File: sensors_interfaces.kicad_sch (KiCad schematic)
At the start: 39 parts, among them IC1 PCF8563T_5,518, IC2 W25Q128JVSIQTR, IC5 SP3485EN-L_TR, IC8 STK8321, U1 TMP112xxDRL, U2 DAC5571IDBVR, U3 DAC5571IDBVR, X14 CH340G, X2 32.768 kHz, X3 TF-15×15, X4 CR1220-2ZX, Y1 X322512MSB4SI

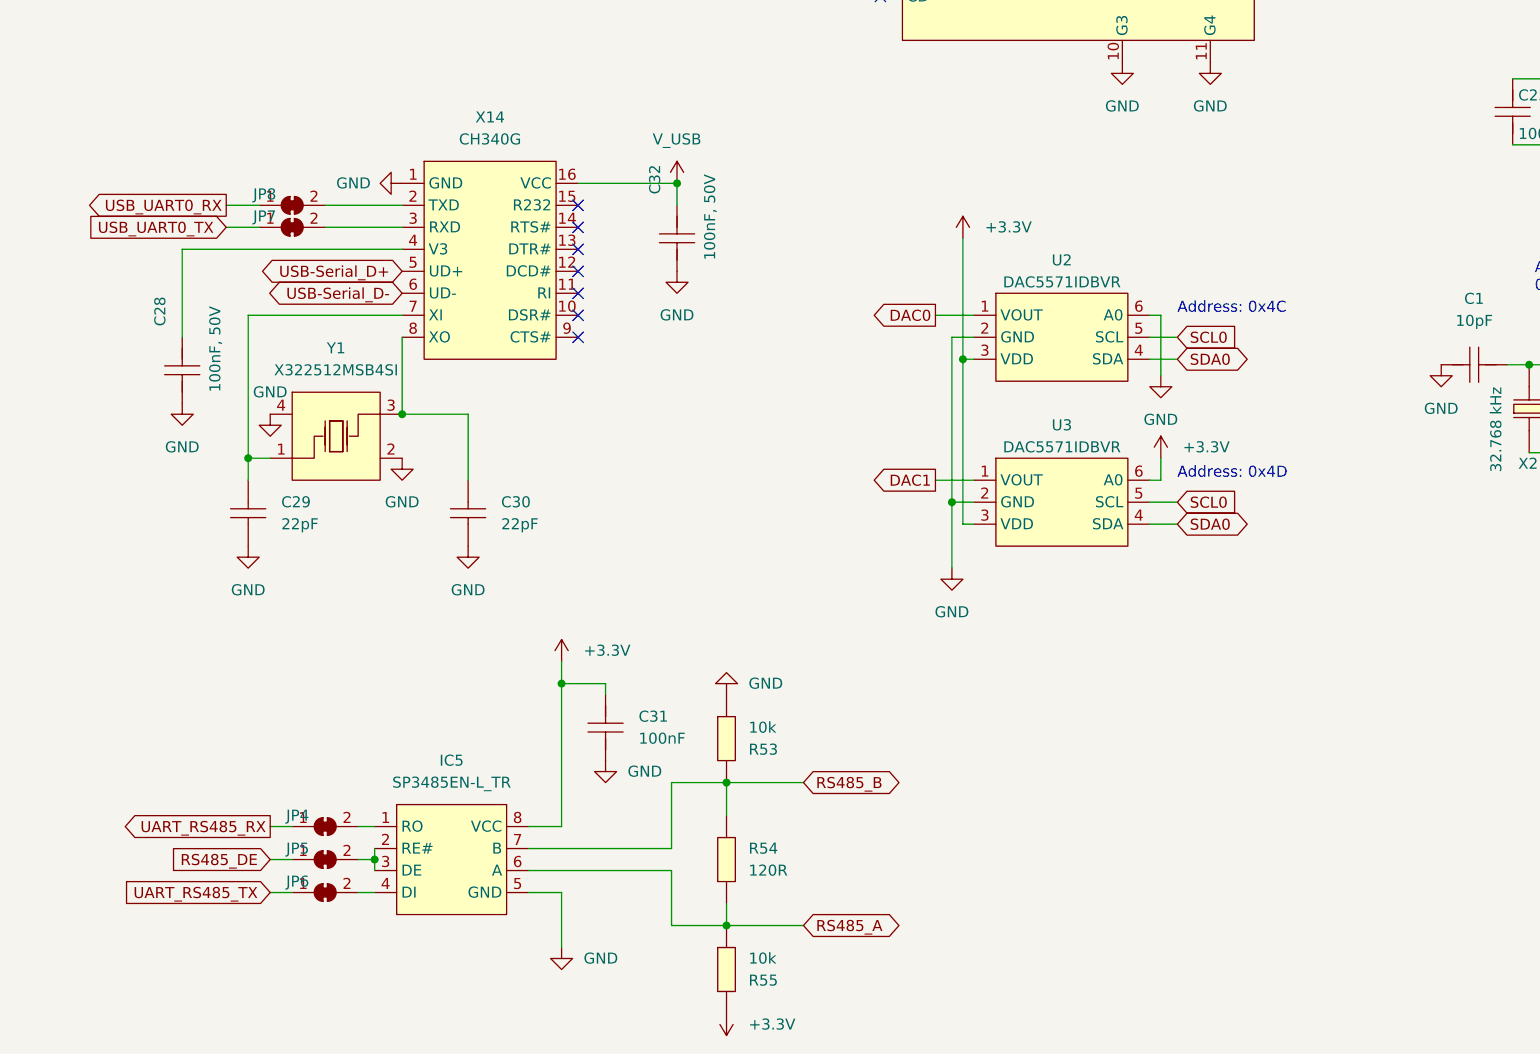
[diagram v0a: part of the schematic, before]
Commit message: Sort out RX/TX problems, improve DAC Circuits, Improve Board Text, switch out certain solder-jumpers with resistors
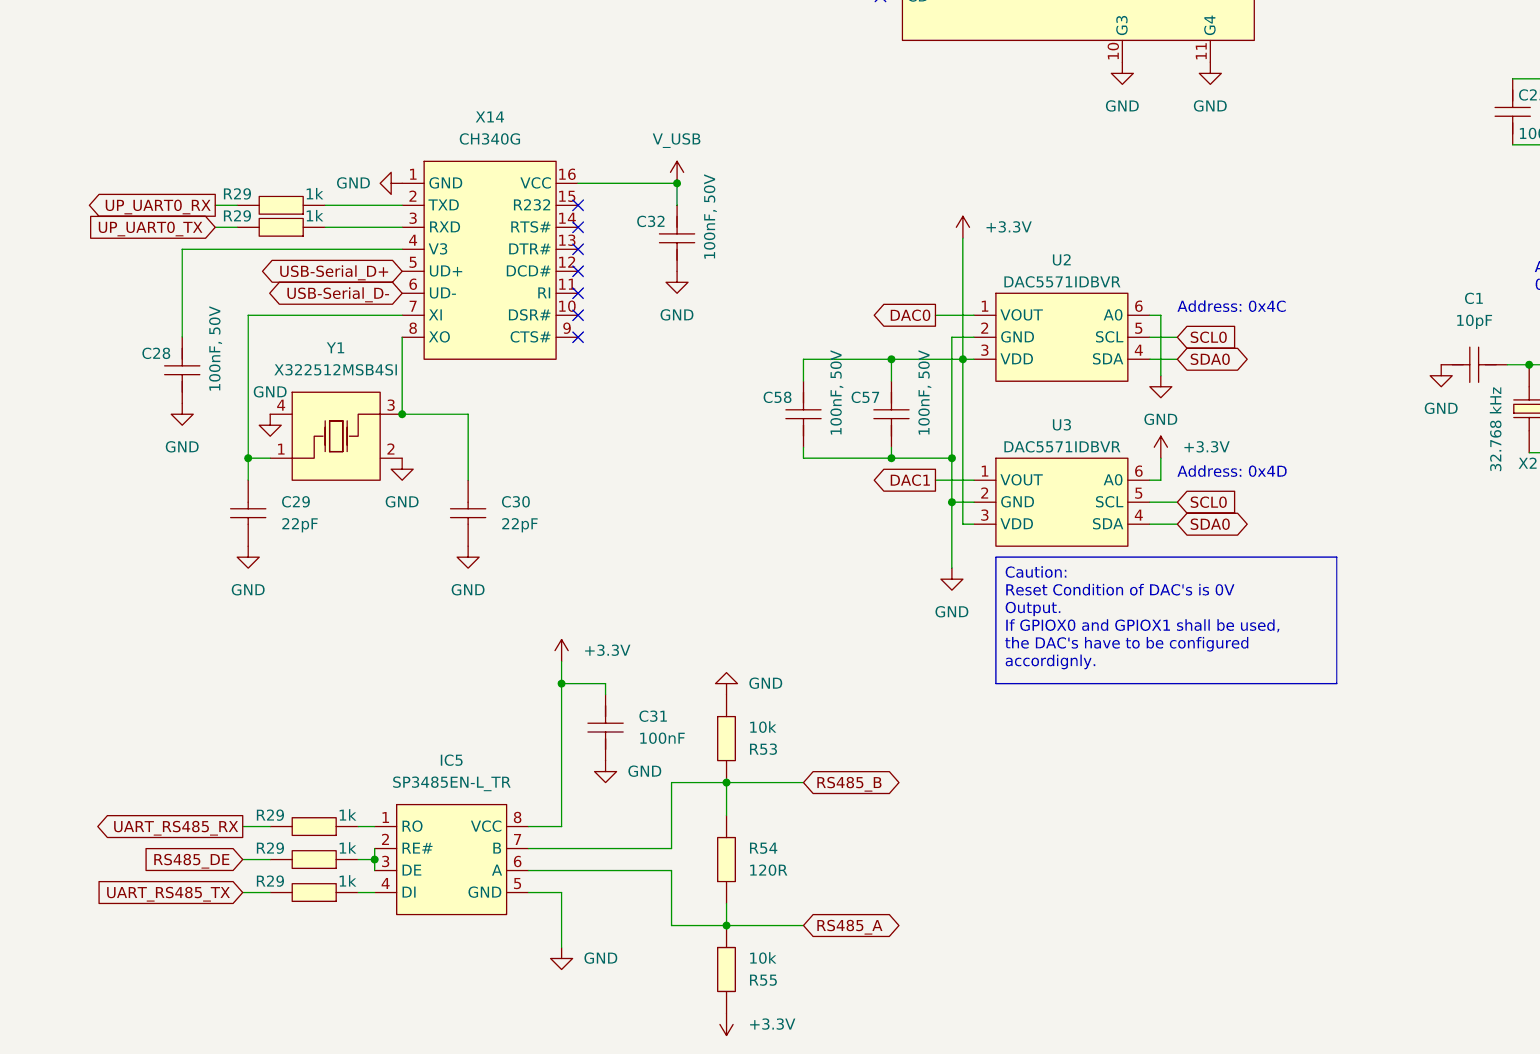
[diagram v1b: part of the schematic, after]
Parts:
- removed JP4, JP5, JP6, JP7, JP8: SolderJumper_2_Bridged, Jumper:SolderJumper-2_P1.3mm_Bridged_Pad1.0x1.5mm, symbol Jumper:SolderJumper_2_Bridged
- added C57, C58: 100nF, 50V, Capacitor_SMD:C_0402_1005Metric_Pad0.74x0.62mm_HandSolder, symbol eduboardv2:CL05B104KB54PNC
- added R29 (x5): 1k, Resistor_SMD:R_0402_1005Metric_Pad0.72x0.64mm_HandSolder, symbol eduboardv2:0402WGF1001TCE
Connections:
- net +3.3V: now also C57.2, C58.2
- net GND: now also C57.1, C58.1
- net RS485_DE: now also R29.2
- net UART_RS485_RX: now also R29.2
- net UART_RS485_TX: now also R29.2
- net at IC5.1 (RO): now also R29.1
- net at IC5.2 (RE#), IC5.3 (DE): now also R29.1
- net at IC5.4 (DI): now also R29.1
- net at X14.3 (RXD): now also R29.1
- net at X14.2 (TXD): now also R29.1
- new net UP_UART0_RX: R29.2
- new net UP_UART0_TX: R29.2

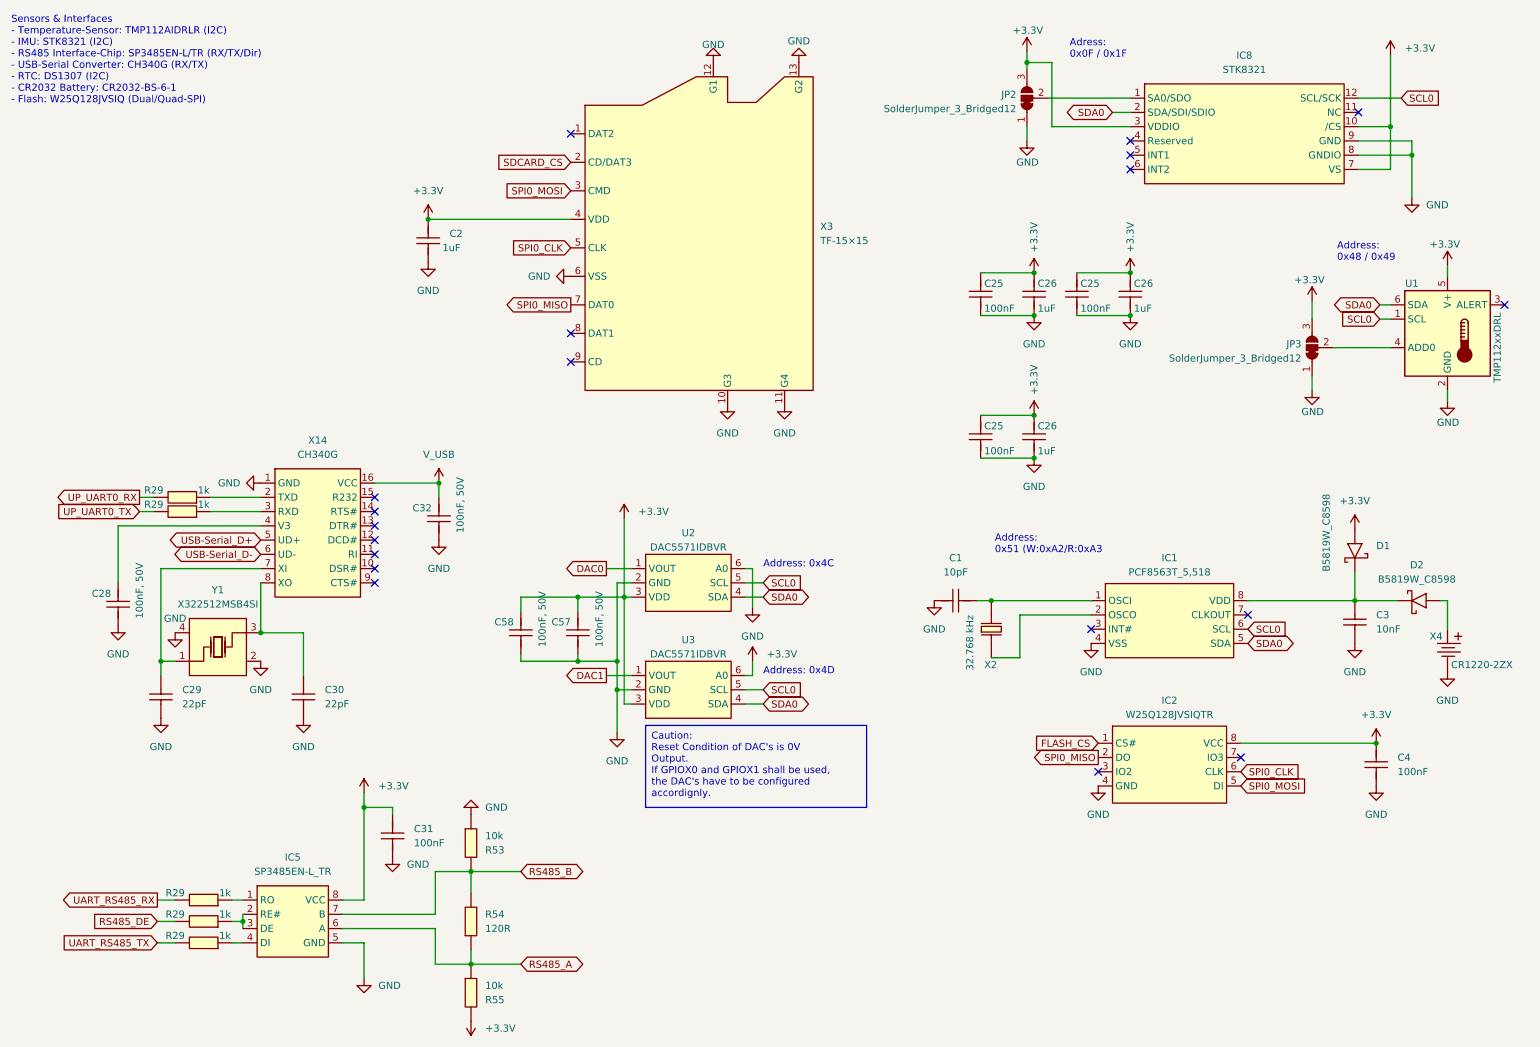
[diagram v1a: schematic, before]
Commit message: replace DAC with SPI Variant. Set Version to 2.2
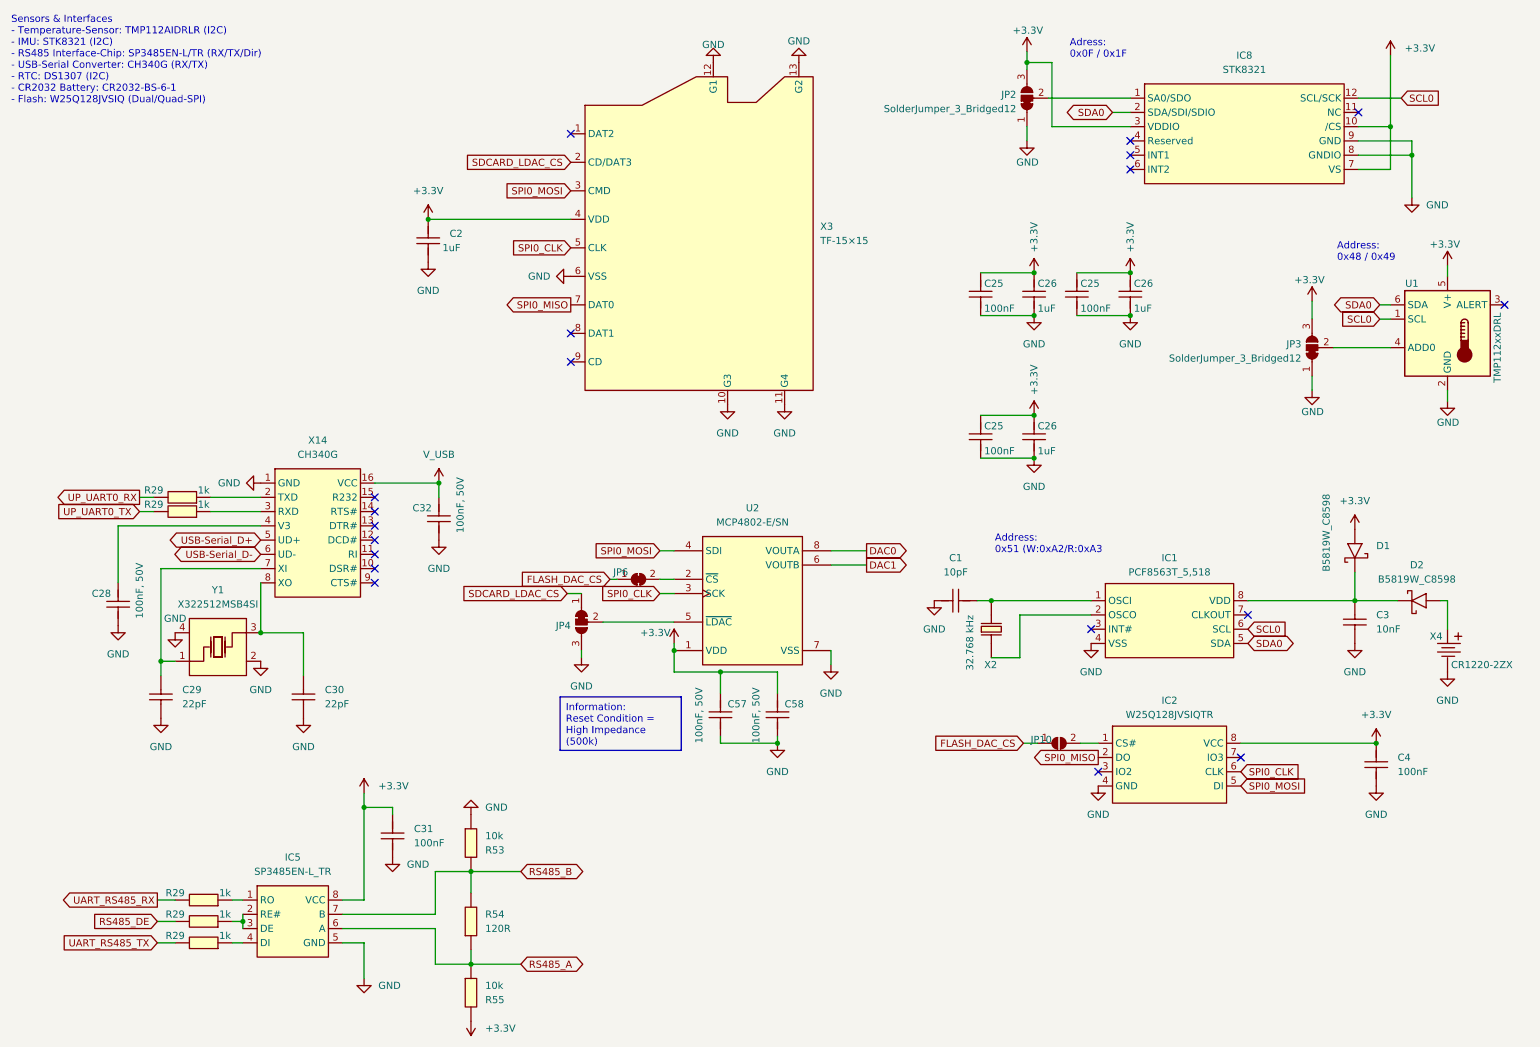
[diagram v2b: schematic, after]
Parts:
- removed U2, U3: DAC5571IDBVR, EduboardV2_kicadlib:SOT-23-6_L2.9-W1.6-P0.95-LS2.8-BR, symbol EduboardV2_kicadlib:DAC5571IDBVR
- added JP10: SolderJumper_2_Open, Jumper:SolderJumper-2_P1.3mm_Open_Pad1.0x1.5mm, symbol Jumper:SolderJumper_2_Open
- added JP4: SolderJumper_3_Bridged12, Jumper:SolderJumper-3_P1.3mm_Bridged12_Pad1.0x1.5mm, symbol Jumper:SolderJumper_3_Bridged12
- added JP6: SolderJumper_2_Bridged, Jumper:SolderJumper-2_P1.3mm_Bridged_Pad1.0x1.5mm, symbol Jumper:SolderJumper_2_Bridged
- added U2: MCP4802-E/SN, EduboardV2_kicadlib:SOIC-8_L4.9-W3.9-P1.27-LS6.0-BL, symbol EduboardV2_kicadlib:MCP4802-E_SN
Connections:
- net +3.3V: now also U2.1 (VDD)
- net DAC0: now also U2.8 (VOUTA)
- net DAC1: now also U2.6 (VOUTB)
- net GND: now also JP4.3 (B), U2.7 (VSS)
- net SPI0_CLK: now also U2.3 (SCK)
- net SPI0_MOSI: now also U2.4 (SDI)
- net FLASH_CS: no longer names the net of IC2.1 (CS#)
- net FLASH_CS: now also JP10.2 (B)
- net SDCARD_CS renamed SDCARD_LDAC_CS
- net SDCARD_LDAC_CS: now also JP4.1 (A)
- new net: JP4.2 (C), U2.5 (~{LDAC})
- new net: JP6.2 (B), U2.2 (~{CS})
- new net FLASH_DAC_CS: JP10.1 (A), JP6.1 (A)
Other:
- note removed: "Address: 0x4C"
- note removed: "Address: 0x4D"

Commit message: migrate to kicad version 8. Add some alternative part numbers
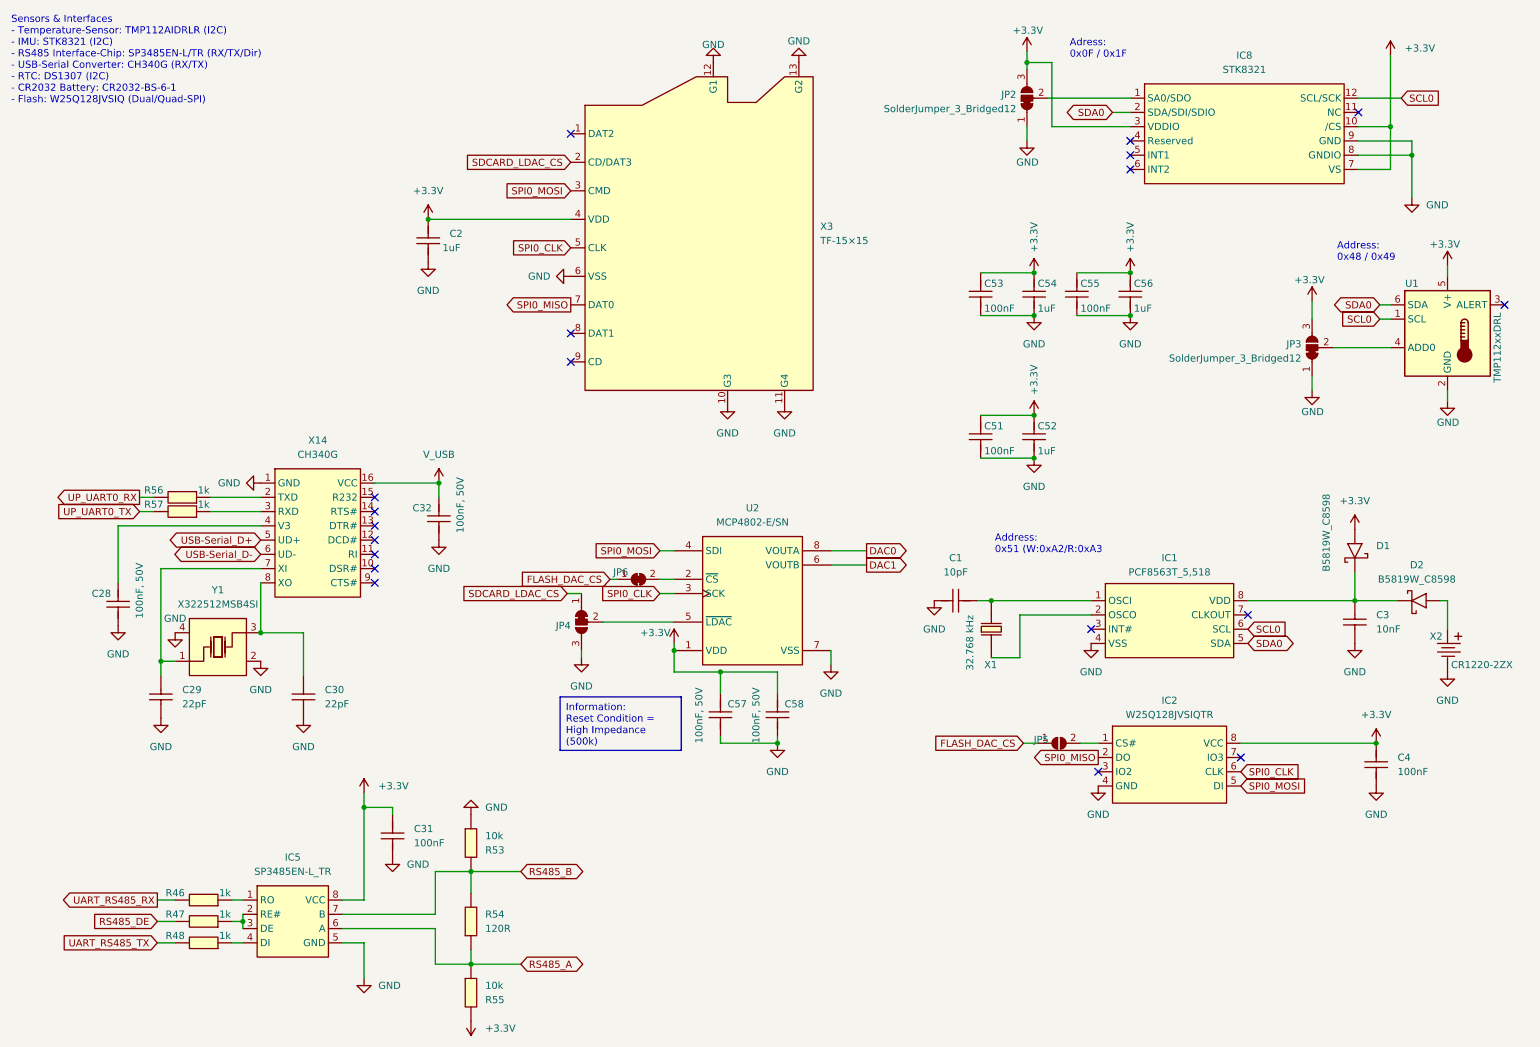
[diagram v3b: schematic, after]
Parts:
- renumbered C25 to C51, C26 to C52, C25 to C53, C26 to C54, C25 to C55, C26 to C56, JP10 to JP5, R29 to R46, R29 to R47, R29 to R48, R29 to R56, R29 to R57, X2 to X1, X4 to X2
